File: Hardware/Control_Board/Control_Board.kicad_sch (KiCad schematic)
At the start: 2 parts, among them U1 ESP32-S2, U3 DRV8231ADSG

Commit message: fleshed out info/planning, roughed in more schematics, added short readme
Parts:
- removed U3: DRV8231ADSG, Package_SON:WSON-8-1EP_2x2mm_P0.5mm_EP0.9x1.6mm, symbol Driver_Motor:DRV8231ADSG
- added J1: DF11CZ-4DP-2V_27_, Meow:DF11CZ4DP2V27, symbol Meow:DF11CZ-4DP-2V_27_
- added J2: DF11CZ-4DP-2V_27_, Meow:DF11CZ6DP2V27, symbol Meow:DF11CZ-6DP-2V_27_
- added J3: DF11CZ-8DP-2V_27_, Meow:DF11CZ8DP2V27, symbol Meow:DF11CZ-8DP-2V_27_
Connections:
- new net Batt PWR: J2.6
- new net GND: J2.2, J2.4, J3.4, J3.6, J3.8
- new net HE 1: J3.2
- new net HE 2: J3.3
- new net HE PWR: J3.1
- new net Jack PWR: J2.1
- new net LED PWR: J3.7
- new net Motor +: J2.3
- new net Motor -: J2.5
- new net Weight PWR: J3.5
- no-connect marks 0 -> 6
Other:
- added sheet Motor (Motor.kicad_sch)
- note added: "OEM Headers"

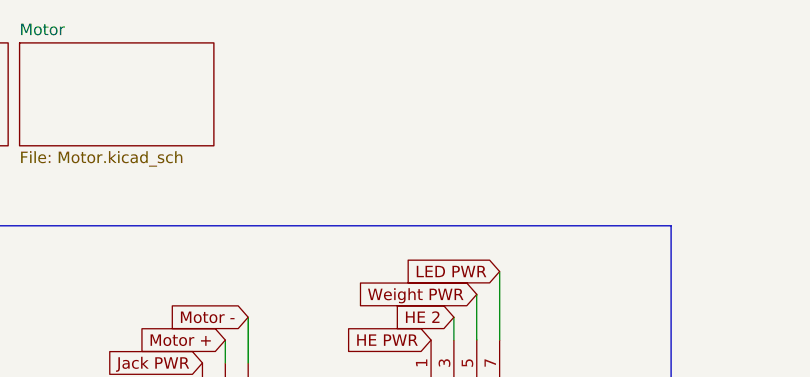
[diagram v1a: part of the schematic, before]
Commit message: took measurements, need to make contact switch for silicon footprint
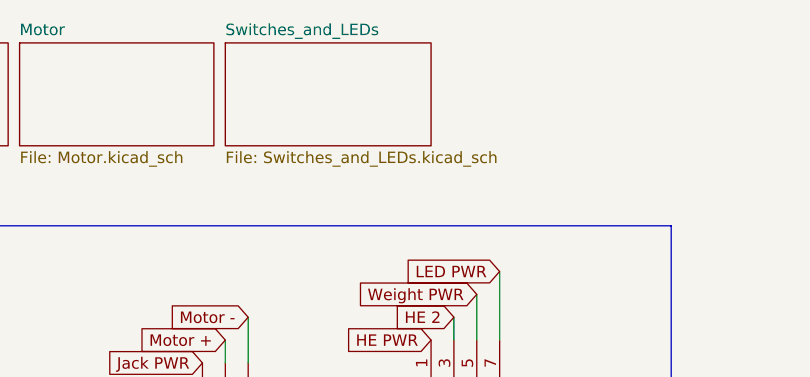
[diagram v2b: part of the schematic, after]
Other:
- added sheet Switches_and_LEDs (Switches_and_LEDs.kicad_sch)
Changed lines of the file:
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@@
+		)
+	)
+	(sheet
+		(at 63.5 19.05)
+		(size 22.86 11.43)
+		(exclude_from_sim no)
+		(in_bom yes)
+		(on_board yes)
+		(dnp no)
+		(fields_autoplaced yes)
+		(stroke
+			(width 0.1524)
+			(type solid)
+		)
+		(fill
+			(color 0 0 0 0)
+		)
+		(property "Sheetname" "Switches_and_LEDs"
+			(at 63.5 18.3384 0)
+			(show_name no)
+			(do_not_autoplace no)
+			(effects
+				(font
+					(size 1.27 1.27)
+				)
+				(justify left bottom)
+			)
+		)
+		(property "Sheetfile" "Switches_and_LEDs.kicad_sch"
+			(at 63.5 31.0646 0)
+			(show_name no)
+			(do_not_autoplace no)
+			(effects
+				(font
+					(size 1.27 1.27)
+				)
+				(justify left top)
+			)
+		)
+		(instances
+			(project "Control_Board"
+				(path "/dfd915fb-cbd4-45ac-acd9-a03ccf310acf"
+					(page "4")
+				)
+			)
 		)
 	)
